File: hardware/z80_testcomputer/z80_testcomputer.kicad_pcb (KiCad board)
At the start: 2 copper layers, 95 x 100 mm, 23 parts, among them J1 Conn_02x15_Odd_Even, J2 Conn_02x15_Odd_Even, J3 Conn_01x32, U1 Z84C000XPEG, U2 SRAM_512K8B_DIP_SOP_SOJ, U3 EEPROM_512K8B_DIP, U4 Z84C200XPEG

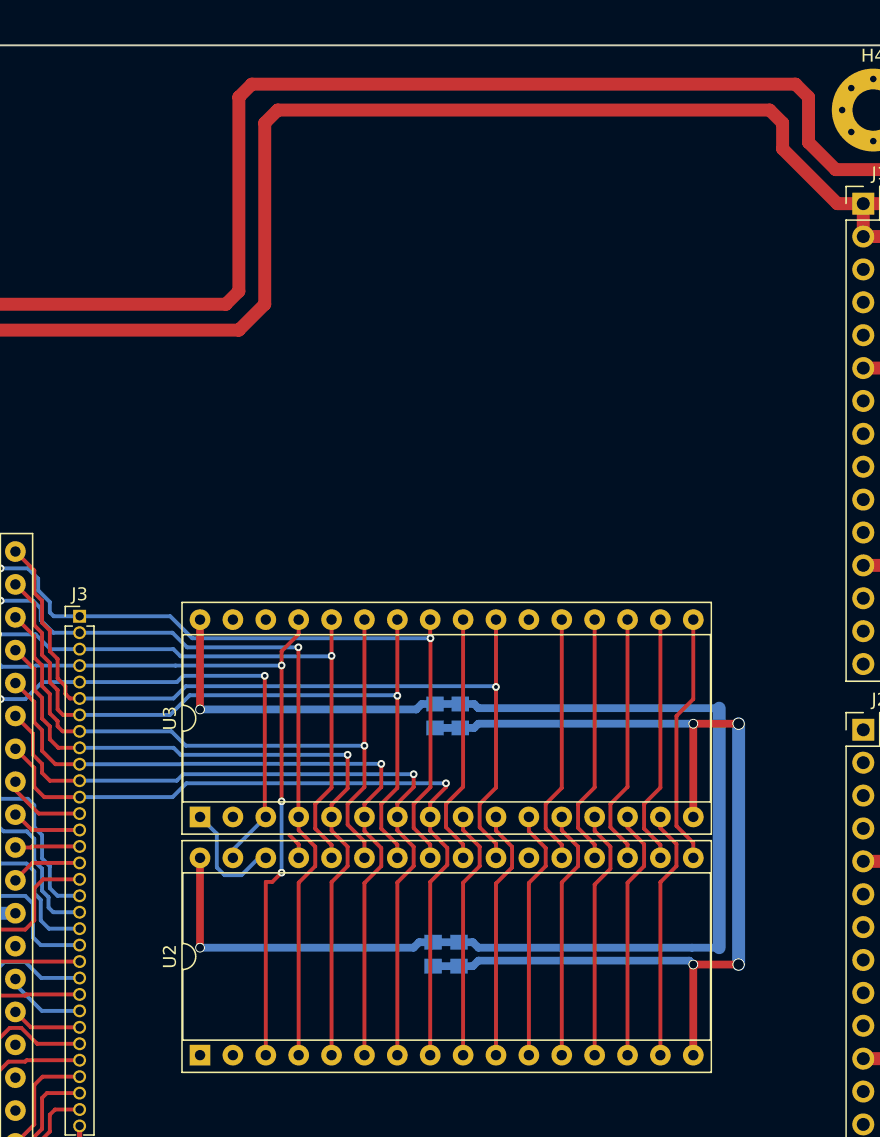
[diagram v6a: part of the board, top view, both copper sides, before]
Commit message: further power and bus routing
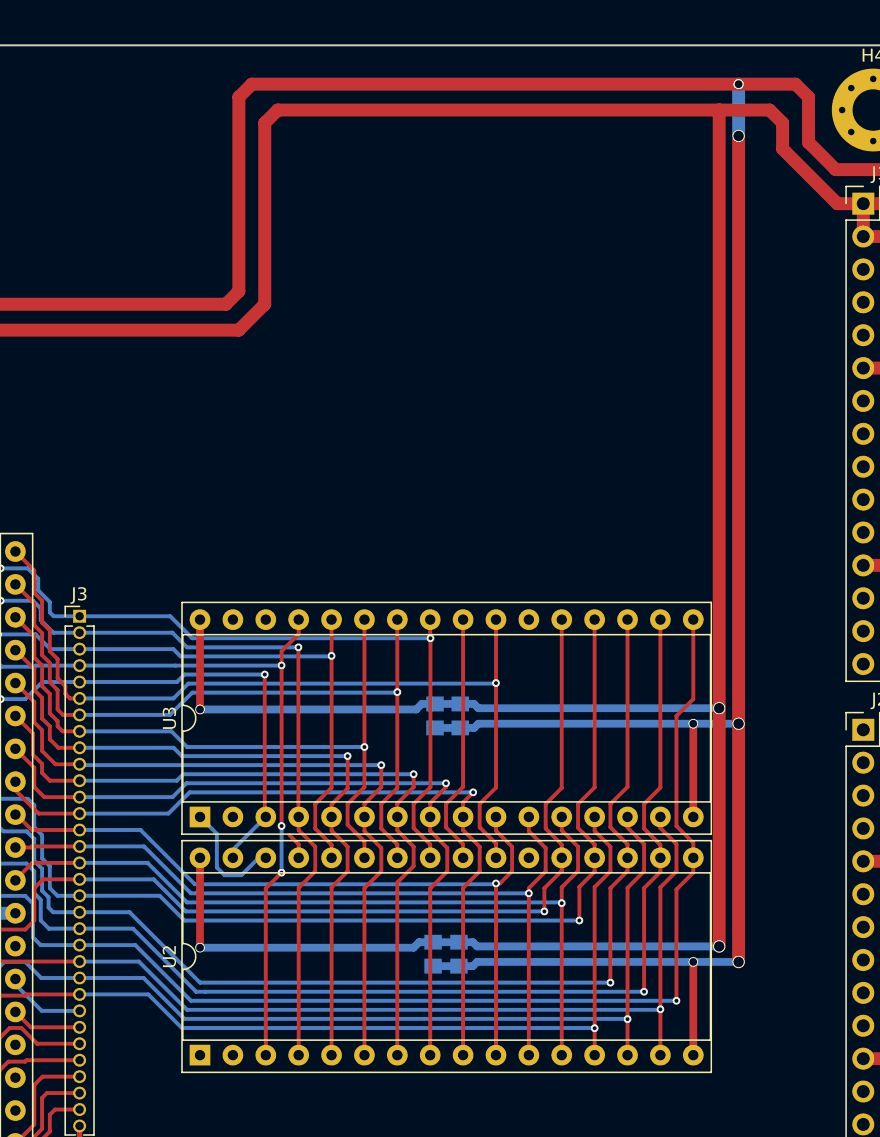
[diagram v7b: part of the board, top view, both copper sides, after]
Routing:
- net /D3: track 51.0 -> 110.5 mm, vias 1 -> 2
- net /D4: track 52.0 -> 108.5 mm, vias 1 -> 2
- net /D5: track 45.3 -> 98.7 mm, vias 1 -> 2
- net /VSS: track 330.1 -> 379.3 mm, vias 5 -> 7
- net /D2: track 41.2 -> 87.6 mm, vias 0 -> 1
- net /VDD: track 273.7 -> 319.7 mm, vias 3 -> 5
- net /D6: track 49.3 -> 94.1 mm, vias 1 -> 2
- net /D1: track 43.3 -> 86.9 mm, vias 1 -> 2
- net /D7: track 43.2 -> 84.9 mm, vias 1 -> 2
- net /D0: track 40.2 -> 81.0 mm, vias 0 -> 1
- net /A0: track 25.0 -> 63.5 mm, vias 0 -> 1
- net /A1: track 24.5 -> 60.7 mm, vias 0 -> 1
- net /A2: track 24.9 -> 59.0 mm, vias 0 -> 1
- net /A3: track 25.8 -> 59.1 mm, vias 0 -> 1

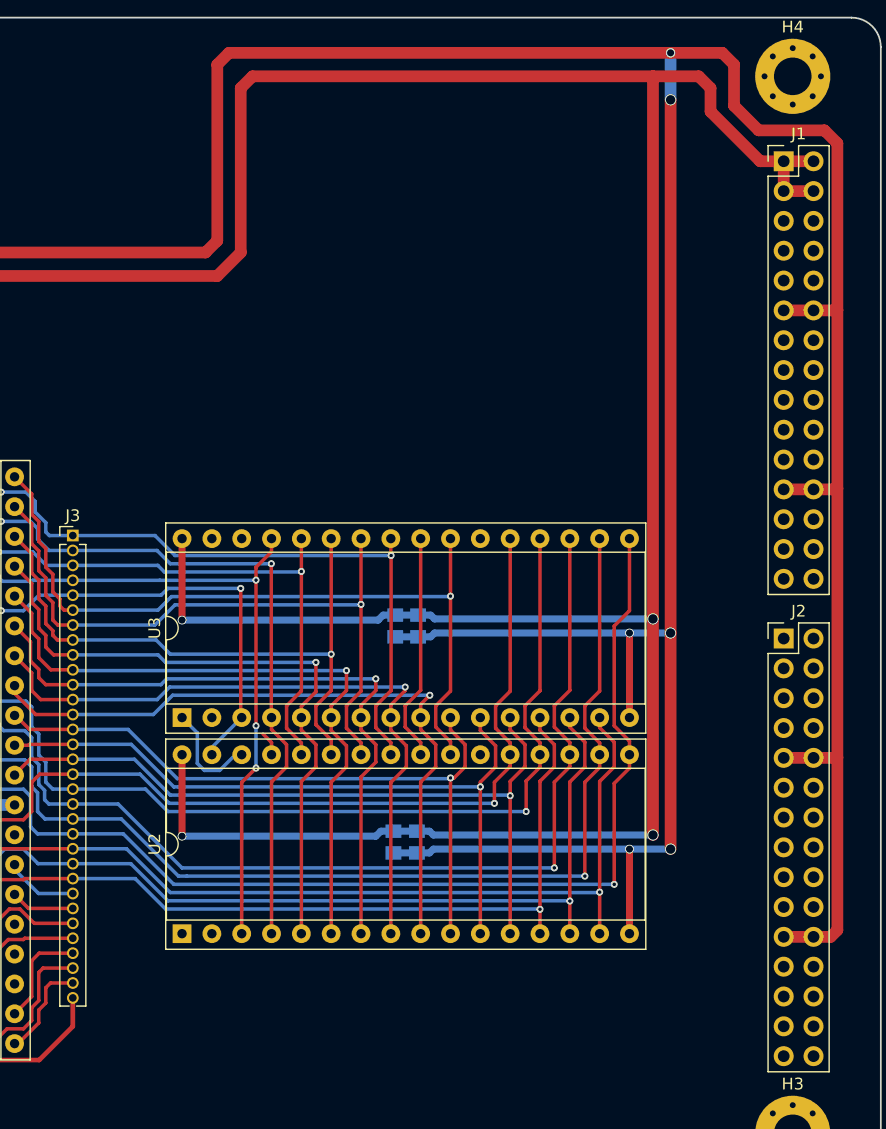
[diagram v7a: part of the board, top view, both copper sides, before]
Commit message: further bus routing, made an error, need to shift a ton of lines
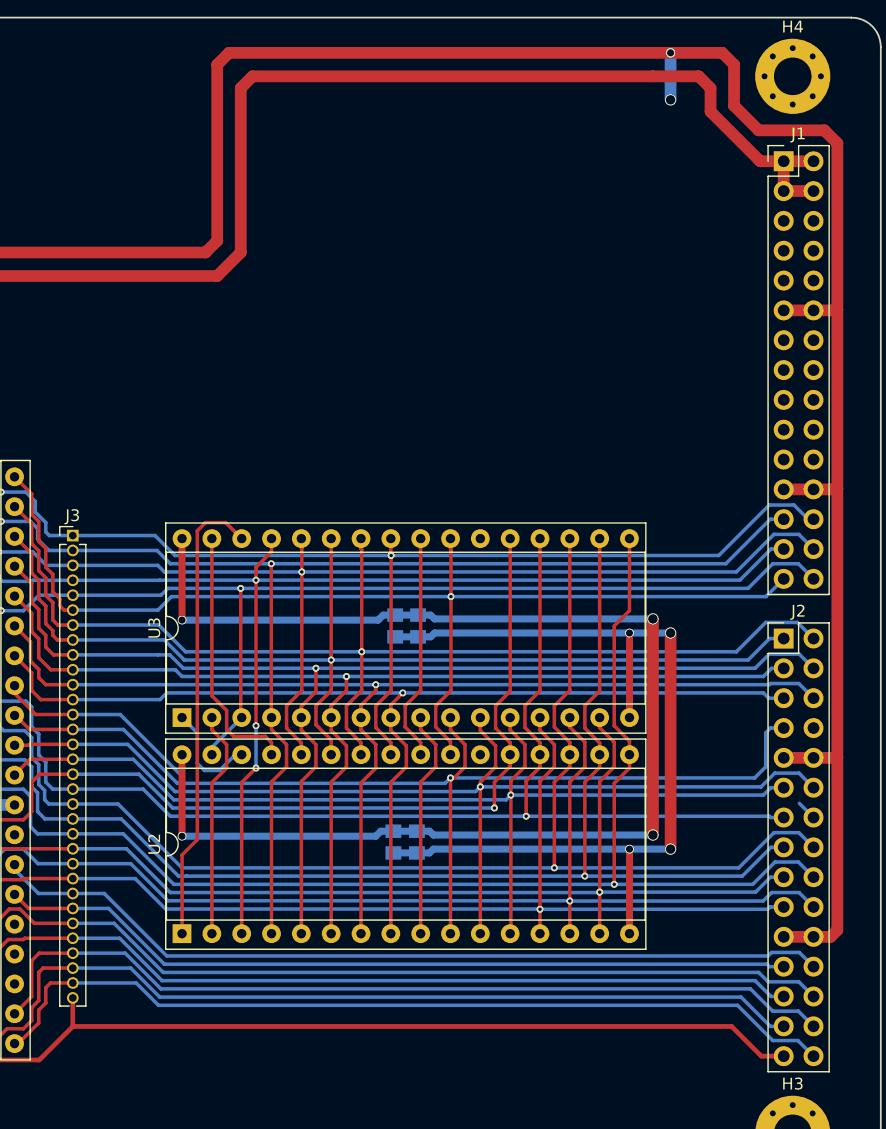
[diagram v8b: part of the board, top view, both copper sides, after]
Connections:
- J1 pad 25: (no net) -> /A12
- J1 pad 26: (no net) -> /A11
- J1 pad 27: (no net) -> /A14
- J1 pad 28: (no net) -> /A13
- J1 pad 29: (no net) -> /A10
- J1 pad 30: (no net) -> /A15
- J2 pad 1: (no net) -> /A8
- J2 pad 11: (no net) -> /A0
- J2 pad 12: (no net) -> /A1
- J2 pad 13: (no net) -> /D6
- J2 pad 14: (no net) -> /D7
- J2 pad 15: (no net) -> /D4
- J2 pad 16: (no net) -> /D5
- J2 pad 17: (no net) -> /D2
- J2 pad 18: (no net) -> /D3
- J2 pad 19: (no net) -> /D0
- J2 pad 2: (no net) -> /A9
- J2 pad 20: (no net) -> /D1
- J2 pad 23: (no net) -> /!RESET
- J2 pad 24: (no net) -> /!M1
- J2 pad 25: (no net) -> /!MREQ
- J2 pad 26: (no net) -> /!INT
- J2 pad 27: (no net) -> /!IORQ
- J2 pad 28: (no net) -> /!WR
- J2 pad 29: (no net) -> /MCLK
- J2 pad 3: (no net) -> /A6
- J2 pad 30: (no net) -> /!RD
- J2 pad 4: (no net) -> /A7
- J2 pad 5: (no net) -> /A4
- J2 pad 6: (no net) -> /A5
- J2 pad 7: (no net) -> /A2
- J2 pad 8: (no net) -> /A3
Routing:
- net /!M1: track 6.22 -> 72.1 mm
- net /!RD: track 8.50 -> 74.2 mm
- net /!WR: track 8.89 -> 74.5 mm
- net /!INT: track 21.2 -> 86.9 mm
- net /!RESET: track 5.45 -> 68.0 mm
- net /!MREQ: track 22.9 -> 85.4 mm
- net /!IORQ: track 24.9 -> 87.5 mm
- net /MCLK: track 64.5 -> 126.0 mm
- net /A15: track 51.0 -> 101.2 mm
- net /VDD: track 319.7 -> 273.5 mm
- net /A14: track 71.1 -> 117.1 mm
- net /A13: track 60.4 -> 105.8 mm
- net /VSS: track 379.3 -> 333.9 mm
- net /A12: track 72.2 -> 117.4 mm
- net /A7: track 56.2 -> 99.2 mm
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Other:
- net class CLK: clearance 0.4 -> 0.3
